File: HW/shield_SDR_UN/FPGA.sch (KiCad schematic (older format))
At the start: 41 parts

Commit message: RF-Frontend balun
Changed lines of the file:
@@
 $Comp
 L 6slx9tqg144:6SLX9TQG144 U?
-U 0 0 5CD877F5
+U 1 1 5CD877F5
 P 8800 4500
 F 0 "U?" H 8400 4650 60  0000 R CNN
@@
 F 3 "" H 7800 3850 60  0000 C CNN
 F 4 "122-1745-ND" H 8800 4500 50  0001 C CNN "digikey"
-	0    8800 4500
+	1    8800 4500
 	1    0    0    -1
 $EndComp
@@
 $Comp
 L Oscillator:ASE-xxxMHz X?
-U 0 0 5CF0FF08
+U 1 1 5CF0FF08
 P 14300 4300
 F 0 "X?" H 14400 4550 50  0000 L CNN
@@
 F 3 "http://www.abracon.com/Oscillators/ASV.pdf" H 14200 4300 50  0001 C CNN
 F 4 "535-11114-1-ND" H 14300 4300 50  0001 C CNN "DIGIKEY"
-	0    14300 4300
+	1    14300 4300
 	1    0    0    -1
 $EndComp
@@
 $Comp
 L Device:C C?
-U 0 0 5CF12739
+U 1 1 5CF12739
 P 13650 4300
 F 0 "C?" H 13765 4346 50  0000 L CNN
@@
 F 2 "Capacitor_SMD:C_0402_1005Metric" H 13688 4150 50  0001 C CNN
 F 3 "~" H 13650 4300 50  0001 C CNN
-	0    13650 4300
+	1    13650 4300
 	1    0    0    -1
 $EndComp
@@
 $Comp
 L Device:R R?
-U 0 0 5CF5FF3D
+U 1 1 5CF5FF3D
 P 14100 1700
 F 0 "R?" H 14170 1746 50  0000 L CNN
@@
 F 2 "Resistor_SMD:R_0603_1608Metric_Pad1.05x0.95mm_HandSolder" V 14030 1700 50  0001 C CNN
 F 3 "~" H 14100 1700 50  0001 C CNN
-	0    14100 1700
+	1    14100 1700
 	1    0    0    -1
 $EndComp
 $Comp
 L Device:R R?
-U 0 0 5CF60693
+U 1 1 5CF60693
 P 15050 1550
 F 0 "R?" H 15120 1596 50  0000 L CNN
@@
 F 2 "Resistor_SMD:R_0603_1608Metric_Pad1.05x0.95mm_HandSolder" V 14980 1550 50  0001 C CNN
 F 3 "~" H 15050 1550 50  0001 C CNN
-	0    15050 1550
+	1    15050 1550
 	1    0    0    -1
 $EndComp
 $Comp
 L Device:R R?
-U 0 0 5CF60FC5
+U 1 1 5CF60FC5
 P 14100 2200
 F 0 "R?" H 14170 2246 50  0000 L CNN
@@
 F 2 "Resistor_SMD:R_0603_1608Metric_Pad1.05x0.95mm_HandSolder" V 14030 2200 50  0001 C CNN
 F 3 "~" H 14100 2200 50  0001 C CNN
-	0    14100 2200
+	1    14100 2200
 	1    0    0    -1
 $EndComp
@@
 $Comp
 L Device:LED D?
-U 0 0 5CFC4A4F
+U 1 1 5CFC4A4F
 P 14100 2700
 F 0 "D?" V 14139 2583 50  0000 R CNN
@@
 F 3 "http://optoelectronics.liteon.com/upload/download/DS22-2000-222/LTST-C191KFKT.pdf" H 14100 2700 50  0001 C CNN
 F 4 "160-1445-1-ND" V 14100 2700 50  0001 C CNN "DIGIKEY"
-	0    14100 2700
+	1    14100 2700
 	0    -1   -1   0
 $EndComp

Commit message: Footprints updated
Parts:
- removed D? (x2): LED, LED_SMD:LED_0805_2012Metric_Pad1.15x1.40mm_HandSolder, symbol Device:LED
- removed R? (x2): 1.8k, Resistor_SMD:R_0603_1608Metric_Pad1.05x0.95mm_HandSolder, symbol Device:R
- added D? (x2): LED, LED_SMD:LED_0805_2012Metric_Pad1.15x1.40mm_HandSolder, symbol Device:LED
- added R? (x2): 470, Resistor_SMD:R_0603_1608Metric_Pad1.05x0.95mm_HandSolder, symbol Device:R
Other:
- note added: "Blue"
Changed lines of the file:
@@
 	10750 6950 10750 6800
-Wire Wire Line
-	9650 2100 9650 1950
 Wire Wire Line
 	9650 1950 9750 1950
@@
 Wire Wire Line
 	9000 6650 9000 6950
-$Comp
-L Device:R R?
-U 1 1 5D3F355A
-P 3450 8650
-F 0 "R?" H 3520 8696 50  0000 L CNN
-F 1 "1.8k" V 3450 8550 50  0000 L CNN
-F 2 "Resistor_SMD:R_0603_1608Metric_Pad1.05x0.95mm_HandSolder" V 3380 8650 50  0001 C CNN
-F 3 "~" H 3450 8650 50  0001 C CNN
-	1    3450 8650
-	1    0    0    -1
-$EndComp
-$Comp
-L power:GND #PWR0149
-U 1 1 5D40658F
-P 3450 8950
-F 0 "#PWR0149" H 3450 8700 50  0001 C CNN
-F 1 "GND" H 3455 8777 50  0000 C CNN
-F 2 "" H 3450 8950 50  0001 C CNN
-F 3 "" H 3450 8950 50  0001 C CNN
-	1    3450 8950
-	1    0    0    -1
-$EndComp
-Wire Wire Line
-	3450 8800 3450 8950
 Text Label 3450 7700 1    50   ~ 0
 BLK_LED1
@@
 Wire Wire Line
 	2550 1200 2550 1000
-$Comp
-L Device:LED D?
-U 1 1 5D23F274
-P 3450 8100
-F 0 "D?" H 3442 7845 50  0000 C CNN
-F 1 "LED" H 3442 7936 50  0000 C CNN
-F 2 "LED_SMD:LED_0805_2012Metric_Pad1.15x1.40mm_HandSolder" H 3450 8100 50  0001 C CNN
-F 3 "~" H 3450 8100 50  0001 C CNN
-	1    3450 8100
-	0    -1   -1   0
-$EndComp
-Wire Wire Line
-	3450 7700 3450 7950
-Wire Wire Line
-	3450 8250 3450 8500
-$Comp
-L Device:R R?
-U 1 1 5D398B89
-P 4000 8650
-F 0 "R?" H 4070 8696 50  0000 L CNN
-F 1 "1.8k" V 4000 8550 50  0000 L CNN
-F 2 "Resistor_SMD:R_0603_1608Metric_Pad1.05x0.95mm_HandSolder" V 3930 8650 50  0001 C CNN
-F 3 "~" H 4000 8650 50  0001 C CNN
-	1    4000 8650
-	1    0    0    -1
-$EndComp
-$Comp
-L power:GND #PWR0156
-U 1 1 5D398B91
-P 4000 8950
-F 0 "#PWR0156" H 4000 8700 50  0001 C CNN
-F 1 "GND" H 4005 8777 50  0000 C CNN
-F 2 "" H 4000 8950 50  0001 C CNN
-F 3 "" H 4000 8950 50  0001 C CNN
-	1    4000 8950
-	1    0    0    -1
-$EndComp
-Wire Wire Line
-	4000 8800 4000 8950
 Text Label 4000 7700 1    50   ~ 0
 BLK_LED2
-$Comp
-L Device:LED D?
-U 1 1 5D398B9D
-P 4000 8100
-F 0 "D?" H 3992 7845 50  0000 C CNN
-F 1 "LED" H 3992 7936 50  0000 C CNN
-F 2 "LED_SMD:LED_0805_2012Metric_Pad1.15x1.40mm_HandSolder" H 4000 8100 50  0001 C CNN
-F 3 "~" H 4000 8100 50  0001 C CNN
-	1    4000 8100
-	0    -1   -1   0
-$EndComp
-Wire Wire Line
-	4000 7700 4000 7950
-Wire Wire Line
-	4000 8250 4000 8500
 Text Label 9000 6950 1    50   ~ 0
 BLK_LED1
@@
 PROGRAM_B
 NoConn ~ 12200 3000
+$Comp
+L Device:LED D?
+U 1 1 5CEA040D
+P 3450 8500
+AR Path="/5CC082AD/5CEA040D" Ref="D?"  Part="1"
+AR Path="/5CFB52DC/5CEA040D" Ref="D?"  Part="1"
+AR Path="/5CC08265/5CEA040D" Ref="D?"  Part="1"
+F 0 "D?" V 3489 8383 50  0000 R CNN
+F 1 "LED" V 3398 8383 50  0000 R CNN
+F 2 "LED_SMD:LED_0805_2012Metric_Pad1.15x1.40mm_HandSolder" H 3450 8500 50  0001 C CNN
+F 3 "http://optoelectronics.liteon.com/upload/download/DS22-2000-239/LTST-S220TBKT.pdf" H 3450 8500 50  0001 C CNN
+F 4 "160-2032-1-ND" V 3450 8500 50  0001 C CNN "Digikey"
+	1    3450 8500
+	0    -1   -1   0
+$EndComp
+$Comp
+L power:GND #PWR?
+U 1 1 5CEA040E
+P 3450 8800
+F 0 "#PWR?" H 3450 8550 50  0001 C CNN
+F 1 "GND" H 3455 8627 50  0000 C CNN
+F 2 "" H 3450 8800 50  0001 C CNN
+F 3 "" H 3450 8800 50  0001 C CNN
+	1    3450 8800
+	1    0    0    -1
+$EndComp
+Wire Wire Line
+	3450 8200 3450 8350
+Wire Wire Line
+	3450 8650 3450 8800
+Text Notes 3300 8650 0    39   ~ 0
+Blue
+Wire Wire Line
+	3450 7700 3450 7900
+$Comp
+L Device:LED D?
+U 1 1 5CEA1FB1
+P 4000 8500
+AR Path="/5CC082AD/5CEA1FB1" Ref="D?"  Part="1"
+AR Path="/5CFB52DC/5CEA1FB1" Ref="D?"  Part="1"
+AR Path="/5CC08265/5CEA1FB1" Ref="D?"  Part="1"
+F 0 "D?" V 4039 8383 50  0000 R CNN
+F 1 "LED" V 3948 8383 50  0000 R CNN
+F 2 "LED_SMD:LED_0805_2012Metric_Pad1.15x1.40mm_HandSolder" H 4000 8500 50  0001 C CNN
+F 3 "http://optoelectronics.liteon.com/upload/download/DS22-2000-239/LTST-S220TBKT.pdf" H 4000 8500 50  0001 C CNN
+F 4 "160-2032-1-ND" V 4000 8500 50  0001 C CNN "Digikey"
+	1    4000 8500
+	0    -1   -1   0
+$EndComp
+$Comp
+L power:GND #PWR?
+U 1 1 5CEA1FB2
+P 4000 8800
+F 0 "#PWR?" H 4000 8550 50  0001 C CNN
+F 1 "GND" H 4005 8627 50  0000 C CNN
+F 2 "" H 4000 8800 50  0001 C CNN
+F 3 "" H 4000 8800 50  0001 C CNN
+	1    4000 8800
+	1    0    0    -1
+$EndComp
+Wire Wire Line
+	4000 8200 4000 8350
+Wire Wire Line
+	4000 8650 4000 8800
+Text Notes 3850 8650 0    39   ~ 0
+Blue
+Wire Wire Line
+	4000 7700 4000 7900
+Wire Wire Line
+	9650 1950 9650 2100
+$Comp
+L Device:R R?
+U 1 1 5CEBF6F1
+P 3450 8050
+F 0 "R?" H 3500 8100 50  0000 L CNN
+F 1 "470" V 3450 7950 50  0000 L CNN
+F 2 "Resistor_SMD:R_0603_1608Metric_Pad1.05x0.95mm_HandSolder" V 3380 8050 50  0001 C CNN
+F 3 "http://www.yageo.com/documents/recent/PYu-RC_Group_51_RoHS_L_10.pdf" H 3450 8050 50  0001 C CNN
+F 4 "311-470GRCT-ND" V 3450 8050 50  0001 C CNN "Digikey"
+	1    3450 8050
+	1    0    0    -1
+$EndComp
+$Comp
+L Device:R R?
+U 1 1 5CEC01C3
+P 4000 8050
+F 0 "R?" H 4050 8100 50  0000 L CNN
+F 1 "470" V 4000 7950 50  0000 L CNN
+F 2 "Resistor_SMD:R_0603_1608Metric_Pad1.05x0.95mm_HandSolder" V 3930 8050 50  0001 C CNN
+F 3 "http://www.yageo.com/documents/recent/PYu-RC_Group_51_RoHS_L_10.pdf" H 4000 8050 50  0001 C CNN
+F 4 "311-470GRCT-ND" V 4000 8050 50  0001 C CNN "Digikey"
+	1    4000 8050
+	1    0    0    -1
+$EndComp
 Wire Bus Line
 	5700 9550 5700 10150

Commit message: OTRA VES FOOTPRINT
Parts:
- removed C? (x18): 0.1uF, Capacitor_SMD:C_0402_1005Metric, symbol Device:C
- removed C?: 0.1uF, symbol Device:C
- removed C? (x10): 4.7uF, Capacitor_SMD:C_0603_1608Metric_Pad1.05x0.95mm_HandSolder, symbol Device:C
- removed R?: 220, Resistor_SMD:R_0603_1608Metric_Pad1.05x0.95mm_HandSolder, symbol Device:R
- added C? (x19): 100nF, Capacitor_SMD:C_0603_1608Metric_Pad1.05x0.95mm_HandSolder, symbol Device:C
- added C? (x10): 4.7uF, Capacitor_SMD:C_0603_1608Metric_Pad1.05x0.95mm_HandSolder, symbol Device:C
- added R?: 220, Resistor_SMD:R_0603_1608Metric_Pad1.05x0.95mm_HandSolder, symbol Device:R
- R?: DESCRPTION (none) -> 220 Ohms ±5% 0.1W, 1/10W; DIGIKEY (none) -> 311-220GRCT-ND
- R?: DESCRIPTION (none) -> 4.7 kOhms ±5% 0.1W; DIGIKEY (none) -> 311-4.7KGRCT-ND
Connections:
- net labels added: GCK0, GCK1
- wire segments 355 -> 357
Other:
- note added: "SI351C"

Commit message: OTRA VES FOOTPRINT_v1
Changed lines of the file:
@@
 $Comp
 L Device:R R?
-U 0 0 5CF5FF3D
+U 1 1 5CF5FF3D
 P 14100 1700
 F 0 "R?" H 14170 1746 50  0000 L CNN
@@
 F 4 "311-220GRCT-ND" H 14100 1700 50  0001 C CNN "DIGIKEY"
 F 5 "220 Ohms ±5% 0.1W, 1/10W" H 14100 1700 50  0001 C CNN "DESCRPTION"
-	0    14100 1700
+	1    14100 1700
 	1    0    0    -1
 $EndComp
 $Comp
 L Device:R R?
-U 0 0 5CF60693
+U 1 1 5CF60693
 P 15050 1550
 F 0 "R?" H 15120 1596 50  0000 L CNN
@@
 F 4 "311-4.7KGRCT-ND" H 15050 1550 50  0001 C CNN "DIGIKEY"
 F 5 "4.7 kOhms ±5% 0.1W" H 15050 1550 50  0001 C CNN "DESCRIPTION"
-	0    15050 1550
+	1    15050 1550
 	1    0    0    -1
 $EndComp
@@
 $Comp
 L Device:R R?
-U 0 0 5CF34B67
+U 1 1 5CF34B67
 P 14100 2200
 F 0 "R?" H 14170 2246 50  0000 L CNN
@@
 F 4 "311-220GRCT-ND" H 14100 2200 50  0001 C CNN "DIGIKEY"
 F 5 "220 Ohms ±5% 0.1W, 1/10W" H 14100 2200 50  0001 C CNN "DESCRPTION"
-	0    14100 2200
-	1    0    0    -1
-$EndComp
+	1    14100 2200
+	1    0    0    -1
+$EndComp

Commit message: RF-Front-end connections
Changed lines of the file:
@@
 3V3 FPGA
 $Comp
-L power:GND #PWR?
+L power:GND #PWR0212
 U 1 1 5CF18886
 P 13900 4750
-F 0 "#PWR?" H 13900 4500 50  0001 C CNN
+F 0 "#PWR0212" H 13900 4500 50  0001 C CNN
 F 1 "GND" H 13905 4577 50  0000 C CNN
 F 2 "" H 13900 4750 50  0001 C CNN
@@
 Connection ~ 14900 3100
 $Comp
-L power:GND #PWR?
+L power:GND #PWR0213
 U 1 1 5CFC8B6B
 P 14500 3250
-F 0 "#PWR?" H 14500 3000 50  0001 C CNN
+F 0 "#PWR0213" H 14500 3000 50  0001 C CNN
 F 1 "GND" H 14505 3077 50  0000 C CNN
 F 2 "" H 14500 3250 50  0001 C CNN
@@
 Wire Wire Line
 	15050 1150 15050 1400
-Text GLabel 14450 900  0    50   Input ~ 0
-1V2 FPGA
 Wire Wire Line
 	14450 900  14600 900
@@
 $EndComp
 $Comp
-L power:GND #PWR?
+L power:GND #PWR0214
 U 1 1 5CEA040E
 P 3450 8800
-F 0 "#PWR?" H 3450 8550 50  0001 C CNN
+F 0 "#PWR0214" H 3450 8550 50  0001 C CNN
 F 1 "GND" H 3455 8627 50  0000 C CNN
 F 2 "" H 3450 8800 50  0001 C CNN
@@
 $EndComp
 $Comp
-L power:GND #PWR?
+L power:GND #PWR0215
 U 1 1 5CEA1FB2
 P 4000 8800
-F 0 "#PWR?" H 4000 8550 50  0001 C CNN
+F 0 "#PWR0215" H 4000 8550 50  0001 C CNN
 F 1 "GND" H 4005 8627 50  0000 C CNN
 F 2 "" H 4000 8800 50  0001 C CNN
@@
 	1    0    0    -1
 $EndComp
+Text GLabel 14450 900  0    50   Input ~ 0
+3V3 FPGA
 Wire Bus Line
 	5700 9550 5700 10150

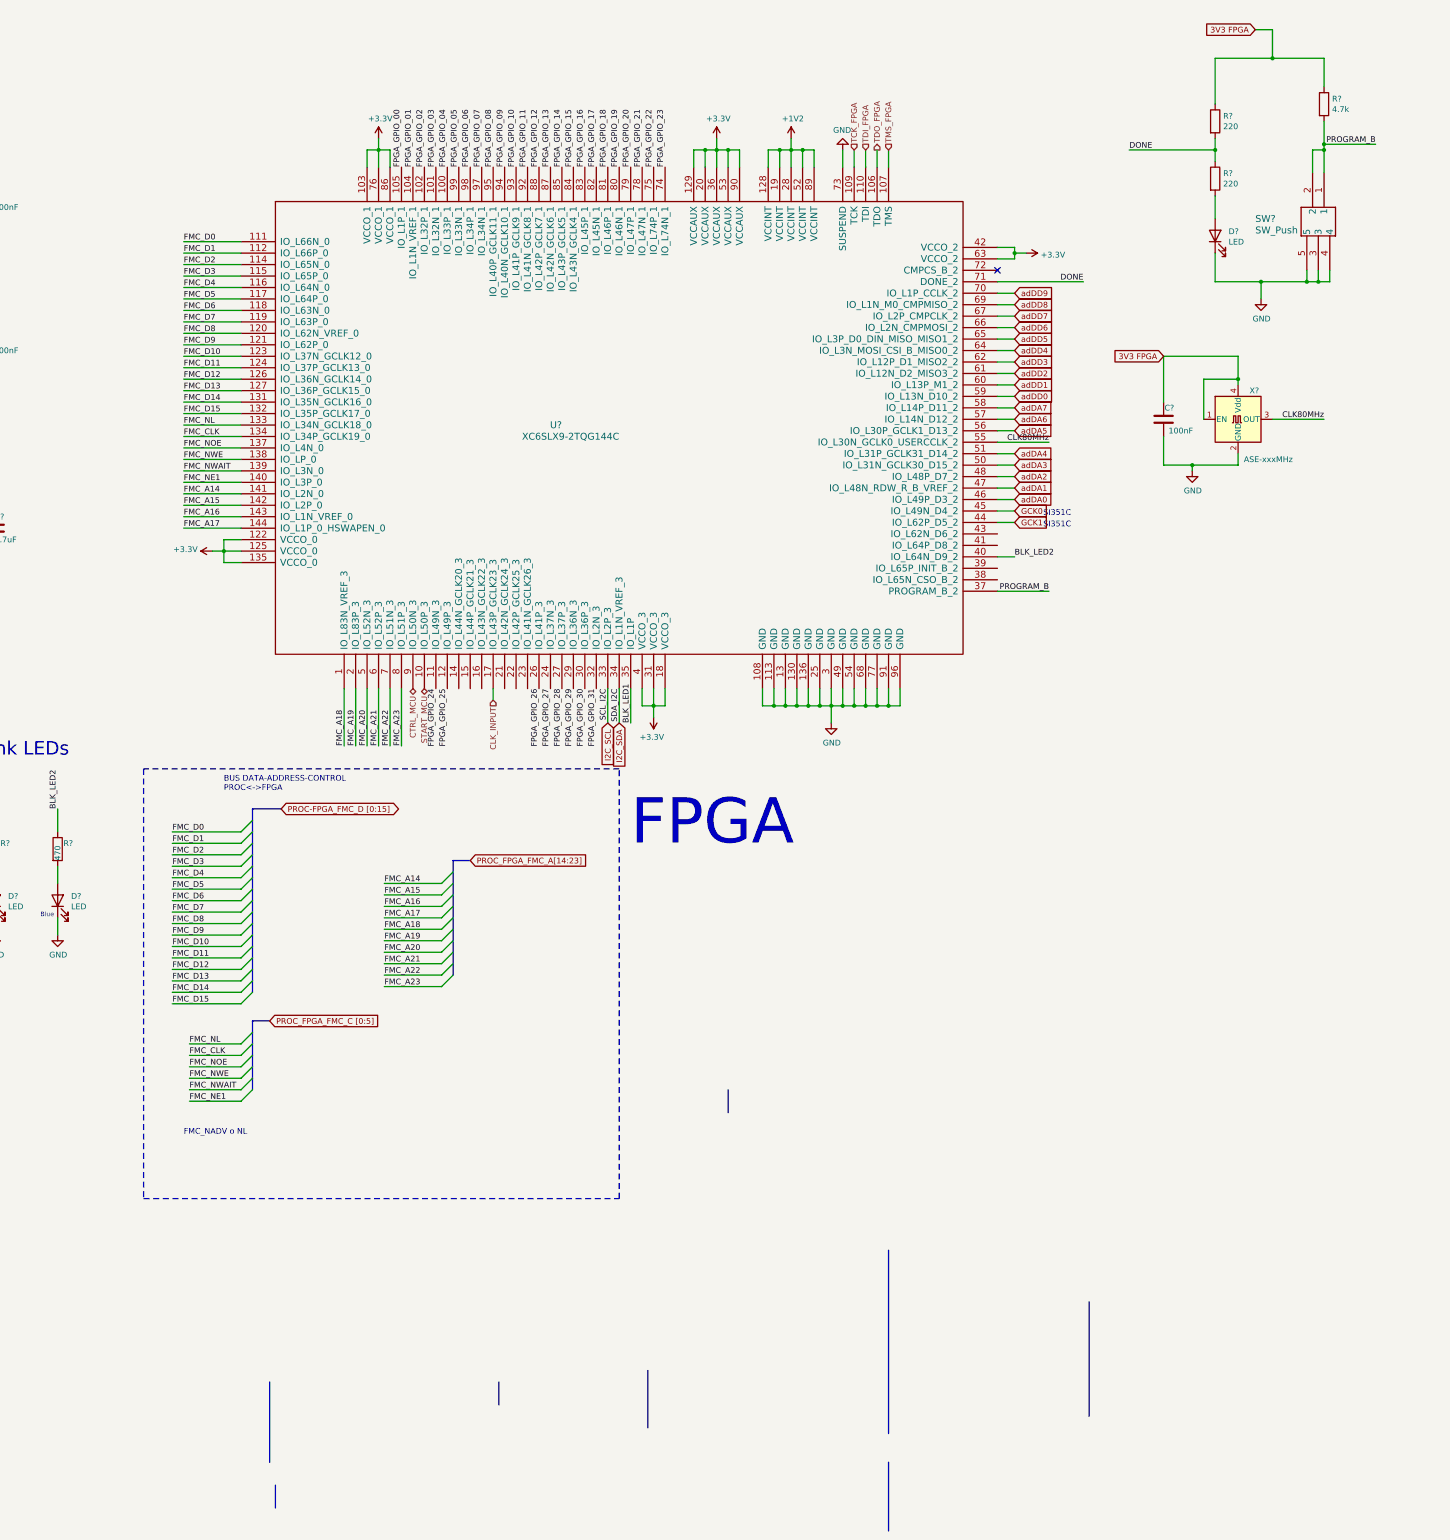
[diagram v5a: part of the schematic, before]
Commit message: JTAG routed
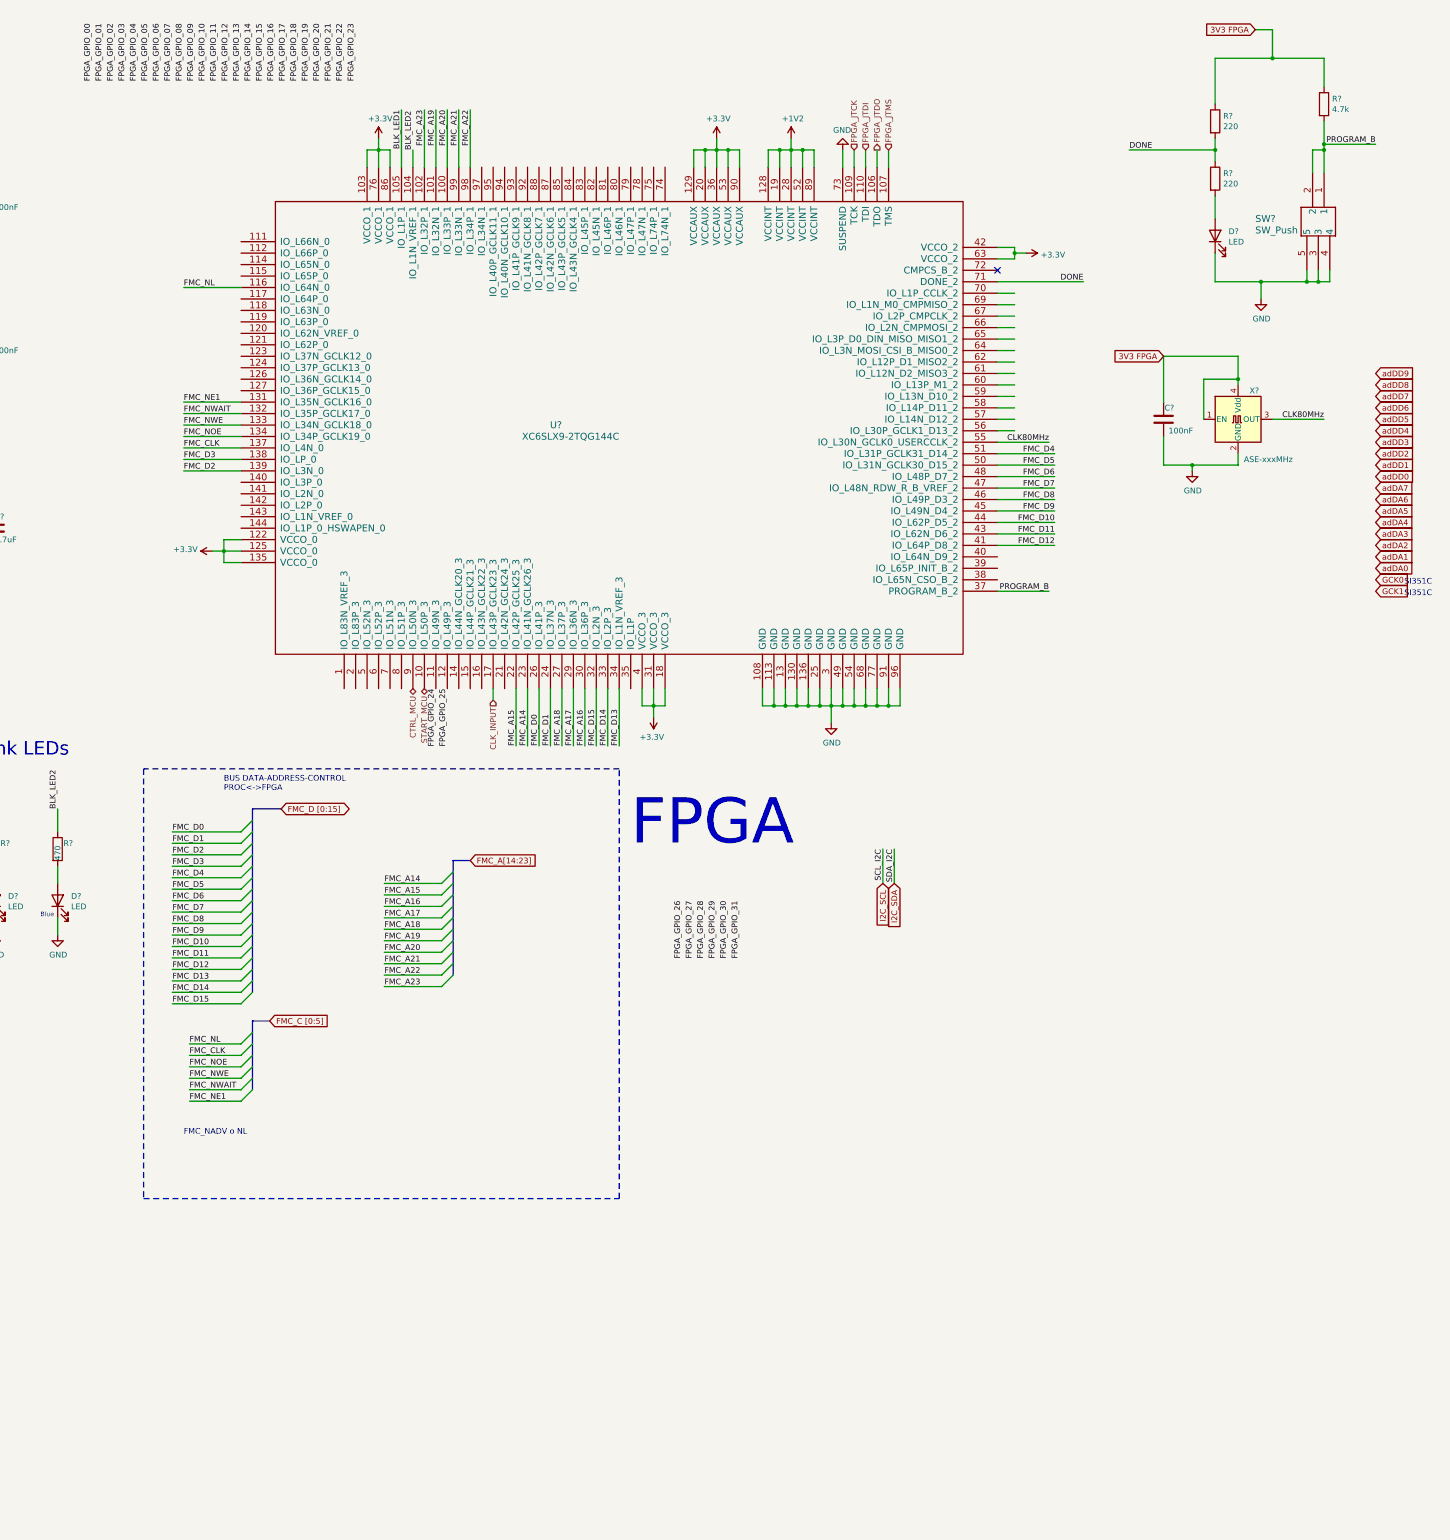
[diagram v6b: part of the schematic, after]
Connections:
- net labels added: FMC_A[14:23], FMC_C [0:5], FMC_D [0:15], FPGA_JTCK, FPGA_JTDI, FPGA_JTDO, FPGA_JTMS
- net labels removed: PROC-FPGA_FMC_D [0:15], PROC_FPGA_FMC_A[14:23], PROC_FPGA_FMC_C [0:5], TCK_FPGA, TDI_FPGA, TDO_FPGA, TMS_FPGA
- wire segments 357 -> 350

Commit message: i2c_complete
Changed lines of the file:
@@
 Text HLabel 7100 6650 3    50   BiDi ~ 0
 CTRL_MCU
-Text Label 11200 8050 3    50   ~ 0
+Text Label 5400 3050 2    50   ~ 0
 SCL_I2C
-Text Label 11300 8050 3    50   ~ 0
+Text Label 5400 2950 2    50   ~ 0
 SDA_I2C
 Text Label 3450 7700 1    50   ~ 0
 BLK_LED1
-Wire Wire Line
-	11300 8050 11300 8350
-Wire Wire Line
-	11200 8050 11200 8350
 $Comp
 L Connector_Generic:Conn_02x18_Counter_Clockwise J?
@@
 Text Notes 1550 7250 0    118  ~ 0
 GPIO Pins
-Text GLabel 11200 8350 3    50   Input ~ 0
-I2C_SCL
-Text GLabel 11300 8350 3    50   Input ~ 0
-I2C_SDA
 $Comp
 L power:+3.3V #PWR0154
@@
 Text Label 8800 7150 1    50   ~ 0
 FMC_D14
+Text GLabel 5100 3050 0    50   Input ~ 0
+I2C_SCL
+Text GLabel 5100 2950 0    50   Input ~ 0
+I2C_SDA
+Wire Wire Line
+	5100 2950 5600 2950
+Wire Wire Line
+	5100 3050 5600 3050
 Wire Bus Line
 	5700 9550 5700 10150
